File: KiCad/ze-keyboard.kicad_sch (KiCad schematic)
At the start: 25 parts, among them J1 AVR-ISP-6, SW1 SW_Push, SW2 SW_Push_Reset, SW3 SW_Push, U1 ATmega32U4-A, U2 PRTR5V0U2X, Y1 Crystal_GND24_Small

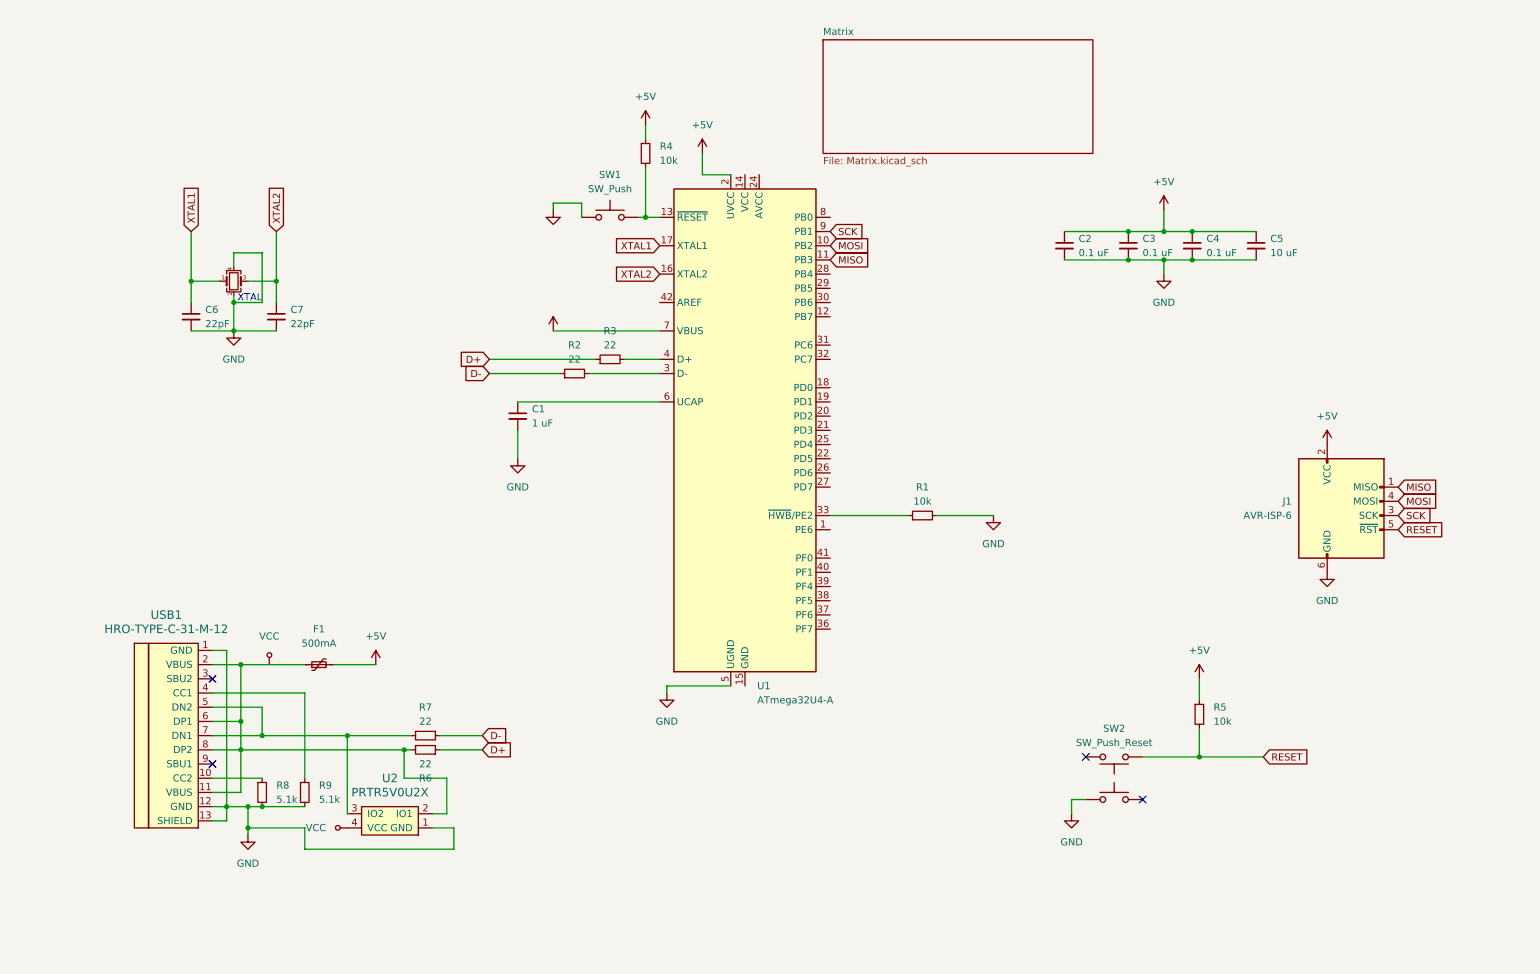
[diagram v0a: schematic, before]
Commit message: "finish" the keyboard schematics
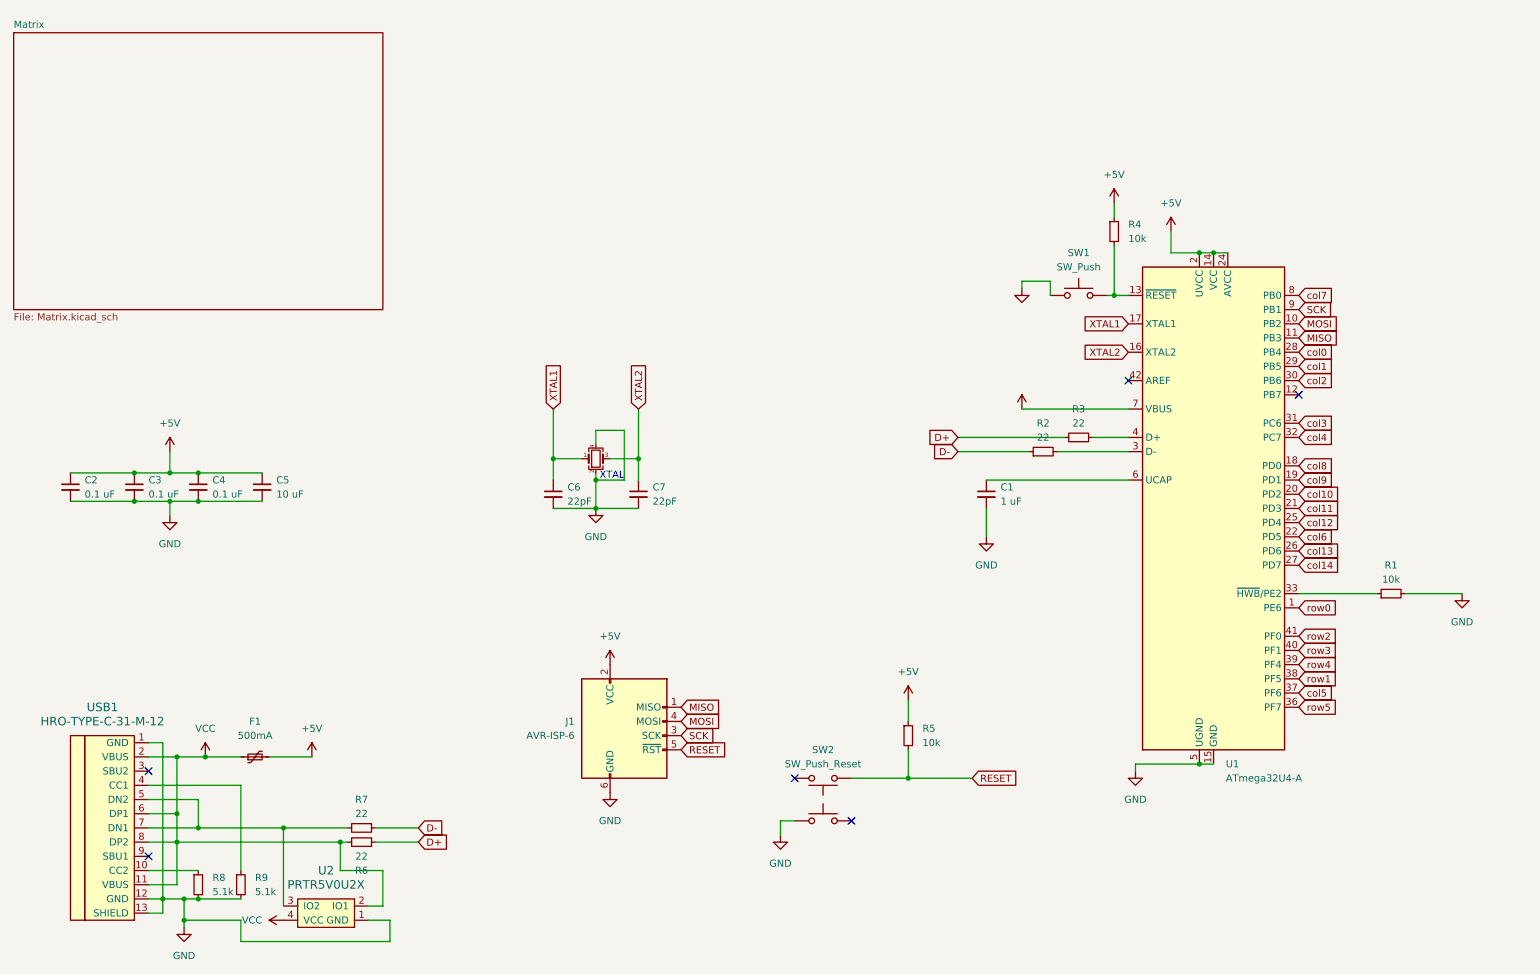
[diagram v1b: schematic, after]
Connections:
- net +5V: now also U1.14 (VCC), U1.24 (AVCC), U1.34 (VCC), U1.44 (AVCC)
- net GND: now also U1.15 (GND), U1.23 (GND), U1.35 (GND), U1.43 (GND)
- net VCC: now also F1.1, R6.2, U2.2 (IO1), USB1.11 (VBUS), USB1.2 (VBUS), USB1.6 (DP1), USB1.8 (DP2)
- net row0: now reaches U1.1 (PE6)
- net col8: now reaches U1.18 (PD0)
- net col9: now reaches U1.19 (PD1)
- net col10: now reaches U1.20 (PD2)
- net col11: now reaches U1.21 (PD3)
- net col6: now reaches U1.22 (PD5)
- net col12: now reaches U1.25 (PD4)
- net col13: now reaches U1.26 (PD6)
- net col14: now reaches U1.27 (PD7)
- net col0: now reaches U1.28 (PB4)
- net col1: now reaches U1.29 (PB5)
- net col2: now reaches U1.30 (PB6)
- net col3: now reaches U1.31 (PC6)
- net col4: now reaches U1.32 (PC7)
- net row5: now reaches U1.36 (PF7)
- net col5: now reaches U1.37 (PF6)
- net row1: now reaches U1.38 (PF5)
- net row4: now reaches U1.39 (PF4)
- net row3: now reaches U1.40 (PF1)
- net row2: now reaches U1.41 (PF0)
- net col7: now reaches U1.8 (PB0)
- no-connect marks 4 -> 6
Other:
- moved on the sheet: C1, C2, C3, C4, C5, C6, C7, F1, J1, R1, R2, R3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

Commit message: fix stuff... i forgot the other stuff i added
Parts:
- removed J1: AVR-ISP-6, symbol Connector:AVR-ISP-6
- removed SW3: SW_Push, symbol Switch:SW_Push
- removed U1: ATmega32U4-A, Package_QFP:TQFP-44_10x10mm_P0.8mm, symbol MCU_Microchip_ATmega:ATmega32U4-A
- removed U2: PRTR5V0U2X, symbol random-keyboard-parts:PRTR5V0U2X
- removed USB1: HRO-TYPE-C-31-M-12, symbol Type-C:HRO-TYPE-C-31-M-12
- added C10, C12: 22pF, Capacitor_SMD:C_0402_1005Metric, symbol Device:C_Small
- added C11, C8, C9: 1uF, Capacitor_SMD:C_0402_1005Metric, symbol Device:C_Small
- added C13, C14, C15, C16: 100nF, Capacitor_SMD:C_0402_1005Metric, symbol Device:C_Small
- added J1: Conn_01x05, Connector_PinHeader_2.54mm:PinHeader_1x05_P2.54mm_Vertical, symbol Connector_Generic:Conn_01x05
- added J2: USB_C_Receptacle_USB2.0, Connector_USB:USB_C_Receptacle_HRO_TYPE-C-31-M-12, symbol Connector:USB_C_Receptacle_USB2.0
- added U1: XC6206PxxxMR, Package_TO_SOT_SMD:SOT-23-3, symbol Regulator_Linear:XC6206PxxxMR
- added U2: RP2040, Package_DFN_QFN:QFN-56-1EP_7x7mm_P0.4mm_EP3.2x3.2mm, symbol MCU_RaspberryPi:RP2040
- added U3: W25Q128JVS, Package_SO:SOIC-8_5.23x5.23mm_P1.27mm, symbol Memory_Flash:W25Q128JVS
- added U4: SRV05-4, PCM_marbastlib-various:SOT-23-6-routable, symbol PCM_marbastlib-various:SRV05-4
- C1: value 1 uF -> 1uF; footprint (none) -> Capacitor_SMD:C_0402_1005Metric
- C2: value 0.1 uF -> 100nF; footprint (none) -> Capacitor_SMD:C_0402_1005Metric
- C3: value 0.1 uF -> 10uF; footprint (none) -> Capacitor_SMD:C_0603_1608Metric
- C4: value 0.1 uF -> 1uF; footprint (none) -> Capacitor_SMD:C_0402_1005Metric
- C5: value 10 uF -> 100nF; footprint (none) -> Capacitor_SMD:C_0402_1005Metric
- C6, C7: value 22pF -> 100nF; footprint (none) -> Capacitor_SMD:C_0402_1005Metric
- F1: footprint (none) -> Fuse:Fuse_1206_3216Metric
- R1: value 10k -> 27; footprint (none) -> Resistor_SMD:R_0402_1005Metric
- R2: value 22 -> 27; footprint (none) -> Resistor_SMD:R_0402_1005Metric
- R3, R7: value 22 -> 5.1k; footprint (none) -> Resistor_SMD:R_0402_1005Metric
- R4, R5: value 10k -> 5.1k; footprint (none) -> Resistor_SMD:R_0402_1005Metric
- R6: value 22 -> 1k; footprint (none) -> Resistor_SMD:R_0402_1005Metric
- R8: value 5.1k -> 1k; footprint (none) -> Resistor_SMD:R_0402_1005Metric
- R9: footprint (none) -> Resistor_SMD:R_0402_1005Metric
- SW1: value SW_Push -> Flash; footprint (none) -> Button_Switch_SMD:SW_SPST_TL3342
- SW2: value SW_Push_Reset -> Reset; footprint (none) -> Button_Switch_SMD:SW_SPST_TL3342
- Y1: footprint (none) -> Crystal:Crystal_SMD_3225-4Pin_3.2x2.5mm
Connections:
- net +5V: now also C8.2, U1.3 (VI); no longer C2.1, C3.1, C4.1, C5.1, R4.1, R5.1
- net D+: now also R1.2, J2.A6 (D+), J2.B6 (D+), U4.1 (IO1); no longer R3.1, R6.1
- net D-: now also R2.2, J2.A7 (D-), J2.B7 (D-), U4.6 (IO4); no longer R2.1, R7.1
- net GND: now also R7.2, R9.1, SW2.1, C10.1, C11.2, C12.1, C13.2, C14.2, C15.2, C16.2, C8.1, C9.1, J1.5 (Pin_5), J2.A1 (GND), J2.A12 (GND), J2.B1 (GND), J2.B12 (GND), J2.S1 (SHIELD), U1.1 (GND), U2.19 (TESTEN), U2.57 (GND), U3.4 (GND), U4.2 (VN); no longer R1.2, R8.2, R9.2
- net RESET: now also R4.2, SW2.2, J1.3 (Pin_3), U2.26 (RUN); no longer R5.2, SW2.1
- net at R8.1: now also Y1.1, C10.2
- net at R3.2: now also R5.1
- net at R1.1: now also U2.47 (USB_DP)
- net at SW1.2: now also R6.1; no longer R4.2
- net +1V1: now reaches C1.1
- net +1V1: now also C2.1, C13.1, U2.23 (DVDD), U2.45 (VREG_VOUT), U2.50 (DVDD)
- net VCC renamed Q_SEL
- net Q_SEL: now also R5.2, U2.56 (QSPI_SS), U3.1 (~{CS}); no longer F1.1
- net XTAL1 renamed +3V3
- net +3V3: now also C3.1, C4.1, C5.1, C7.1, R3.1, R4.1, C11.1, C14.1, C15.1, C16.1, C9.2, J1.4 (Pin_4), U1.2 (VO), U2.1 (IOVDD), U2.10 (IOVDD), U2.22 (IOVDD), U2.33 (IOVDD), U2.42 (IOVDD), U2.43 (ADC_AVDD), U2.44 (VREG_IN), U2.48 (USB_VDD), U2.49 (IOVDD), U3.8 (VCC); no longer Y1.1
- net XTAL2 renamed XIN
- net XIN: now also C12.2, U2.20 (XIN); no longer C7.1
- new net: R2.1, U2.46 (USB_DM)
- new net: J2.B5 (CC2), R9.2
- new net: J2.A5 (CC1), R7.1
- new net Q_CLK: U2.52 (QSPI_SCLK), U3.6 (CLK)
- new net Q_IO0: U2.53 (QSPI_SD0), U3.5 (DI(IO0))
- new net Q_IO1: U2.55 (QSPI_SD1), U3.2 (DO(IO1))
- new net Q_IO2: U2.54 (QSPI_SD2), U3.3 (IO2)
- new net Q_IO3: U2.51 (QSPI_SD3), U3.7 (IO3)
- new net SWCLK: J1.1 (Pin_1), U2.24 (SWCLK)
- new net SWD: J1.2 (Pin_2), U2.25 (SWD)
- new net VBUS: F1.1, J2.A4 (VBUS), J2.A9 (VBUS), J2.B4 (VBUS), J2.B9 (VBUS), U4.5 (VP)
- new net XOUT: R8.2, U2.21 (XOUT)
- no-connect marks 6 -> 10
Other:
- note removed: "XTAL"

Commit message: do some tracing
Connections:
- net col0: now also U2.29 (GPIO18)
- net col1: now also U2.30 (GPIO19)
- net col10: now also U2.27 (GPIO16)
- net col11: now also U2.28 (GPIO17)
- net col12: now also U2.14 (GPIO11)
- net col13: now also U2.13 (GPIO10)
- net col14: now also U2.12 (GPIO9)
- net col15: now also U2.11 (GPIO8)
- net col2: now also U2.31 (GPIO20)
- net col3: now also U2.32 (GPIO21)
- net col4: now also U2.34 (GPIO22)
- net col5: now also U2.35 (GPIO23)
- net col6: now also U2.15 (GPIO12)
- net col7: now also U2.16 (GPIO13)
- net col8: now also U2.17 (GPIO14)
- net col9: now also U2.18 (GPIO15)
- net rot1: now also U2.9 (GPIO7)
- net row0: now also U2.7 (GPIO5)
- net row1: now also U2.6 (GPIO4)
- net row2: now also U2.5 (GPIO3)
- net row3: now also U2.4 (GPIO2)
- net row4: now also U2.3 (GPIO1)
- net row5: now also U2.2 (GPIO0)
- net rot0: now reaches U2.8 (GPIO6)

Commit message: finish pcb
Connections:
- net col10: now also U2.6 (GPIO4); no longer U2.27 (GPIO16)
- net col11: now also U2.7 (GPIO5); no longer U2.28 (GPIO17)
- net col12: now also U2.15 (GPIO12); no longer U2.14 (GPIO11)
- net col13: now also U2.16 (GPIO13); no longer U2.13 (GPIO10)
- net col14: now also U2.17 (GPIO14); no longer U2.12 (GPIO9)
- net col15: now also U2.18 (GPIO15); no longer U2.11 (GPIO8)
- net col2: now also U2.34 (GPIO22); no longer U2.31 (GPIO20)
- net col3: now also U2.35 (GPIO23); no longer U2.32 (GPIO21)
- net col4: now also U2.36 (GPIO24); no longer U2.34 (GPIO22)
- net col5: now also U2.37 (GPIO25); no longer U2.35 (GPIO23)
- net col6: now also U2.2 (GPIO0); no longer U2.15 (GPIO12)
- net col7: now also U2.3 (GPIO1); no longer U2.16 (GPIO13)
- net col8: now also U2.4 (GPIO2); no longer U2.17 (GPIO14)
- net col9: now also U2.5 (GPIO3); no longer U2.18 (GPIO15)
- net row0: now also U2.14 (GPIO11); no longer U2.7 (GPIO5)
- net row1: now also U2.13 (GPIO10); no longer U2.6 (GPIO4)
- net row2: now also U2.12 (GPIO9); no longer U2.5 (GPIO3)
- net row3: now also U2.11 (GPIO8); no longer U2.4 (GPIO2)
- net row4: now also U2.27 (GPIO16); no longer U2.3 (GPIO1)
- net row5: now also U2.28 (GPIO17); no longer U2.2 (GPIO0)

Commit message: some changes, a bit more jlcpcb stuff
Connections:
- net rot0: now also U2.9 (GPIO7); no longer U2.8 (GPIO6)
- net rot1: now also U2.8 (GPIO6); no longer U2.9 (GPIO7)
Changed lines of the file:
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@@
     )
   )
-  (global_label "rot1" (shape input) (at 275.59 46.99 0) (fields_autoplaced)
+  (global_label "rot1" (shape input) (at 275.59 44.45 0) (fields_autoplaced)
     (effects (font (size 1.27 1.27)) (justify left))
-    (property "Intersheetrefs" "${INTERSHEET_REFS}" (at 282.4456 46.99 0)
+    (property "Intersheetrefs" "${INTERSHEET_REFS}" (at 282.4456 44.45 0)
       (effects (font (size 1.27 1.27)) (justify left) hide)
     )
@@
     )
   )
-  (global_label "rot0" (shape input) (at 275.59 44.45 0) (fields_autoplaced)
+  (global_label "rot0" (shape input) (at 275.59 46.99 0) (fields_autoplaced)
     (effects (font (size 1.27 1.27)) (justify left))
-    (property "Intersheetrefs" "${INTERSHEET_REFS}" (at 282.4456 44.45 0)
+    (property "Intersheetrefs" "${INTERSHEET_REFS}" (at 282.4456 46.99 0)
       (effects (font (size 1.27 1.27)) (justify left) hide)
     )
